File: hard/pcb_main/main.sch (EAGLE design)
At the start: 19 parts

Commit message: nop
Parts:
- added JP1, JP2, JP3, JP4, JP5, JP6: STAND-OFF, SparkFun:STAND-OFF
- added XP1: 2X10-SHROUDED, connector:2X10-SHROUDED
- added XP2, XP3, XP4, XP5, XP6, XP7, XP8: TYCO-174053(2.54), connector:TYCO-174053(2.54)
- added XP9: TYCO-174049(2.54), connector:TYCO-174049(2.54)
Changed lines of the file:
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@@
 <setting verticaltext="up"/>
 </settings>
-<grid distance="0.1" unitdist="inch" unit="inch" style="lines" multiple="1" display="no" altdistance="0.01" altunitdist="inch" altunit="inch"/>
+<grid distance="0.1" unitdist="inch" unit="inch" style="lines" multiple="1" display="yes" altdistance="0.01" altunitdist="inch" altunit="inch"/>
 <layers>
 <layer number="1" name="Top" color="4" fill="1" visible="no" active="no"/>
@@
 <part name="DA3" library="transistor-fet" deviceset="BTS" device="6143D"/>
 <part name="D1" library="optocoupler" deviceset="TCMT4100" device=""/>
+<part name="JP1" library="SparkFun" deviceset="STAND-OFF" device=""/>
+<part name="JP2" library="SparkFun" deviceset="STAND-OFF" device=""/>
+<part name="JP3" library="SparkFun" deviceset="STAND-OFF" device=""/>
+<part name="JP4" library="SparkFun" deviceset="STAND-OFF" device=""/>
+<part name="JP5" library="SparkFun" deviceset="STAND-OFF" device=""/>
+<part name="JP6" library="SparkFun" deviceset="STAND-OFF" device=""/>
+<part name="XP1" library="connector" deviceset="2X10" device="-SHROUDED"/>
+<part name="XP2" library="connector" deviceset="TYCO-174053" device="(2.54)"/>
+<part name="XP3" library="connector" deviceset="TYCO-174053" device="(2.54)"/>
+<part name="XP4" library="connector" deviceset="TYCO-174053" device="(2.54)"/>
+<part name="XP5" library="connector" deviceset="TYCO-174053" device="(2.54)"/>
+<part name="XP6" library="connector" deviceset="TYCO-174053" device="(2.54)"/>
+<part name="XP7" library="connector" deviceset="TYCO-174053" device="(2.54)"/>
+<part name="XP8" library="connector" deviceset="TYCO-174053" device="(2.54)"/>
+<part name="XP9" library="connector" deviceset="TYCO-174049" device="(2.54)"/>
 </parts>
 <sheets>
@@
 </instance>
 <instance part="U$2" gate="G$1" x="-342.9" y="-15.24"/>
+<instance part="XP1" gate="G$1" x="-309.88" y="142.24" rot="MR0"/>
 </instances>
 <busses>
@@
 <attribute name="PARTNO" x="99.06" y="101.6" size="1.778" layer="96" display="off"/>
 </instance>
+<instance part="XP9" gate="G$1" x="38.1" y="142.24" rot="MR0"/>
 </instances>
 <busses>
@@
 <instance part="D1" gate=".3" x="129.54" y="358.14"/>
 <instance part="D1" gate=".4" x="152.4" y="358.14"/>
+<instance part="XP2" gate="G$1" x="53.34" y="391.16" rot="MR0"/>
+<instance part="XP3" gate="G$1" x="53.34" y="342.9" rot="MR0"/>
+<instance part="XP4" gate="G$1" x="55.88" y="294.64" rot="MR0"/>
+<instance part="XP5" gate="G$1" x="55.88" y="243.84" rot="MR0"/>
+<instance part="XP6" gate="G$1" x="55.88" y="193.04" rot="MR0"/>
+<instance part="XP7" gate="G$1" x="55.88" y="142.24" rot="MR0"/>
+<instance part="XP8" gate="G$1" x="55.88" y="96.52" rot="MR0"/>
 </instances>
 <busses>
@@
 </nets>
 </sheet>
+<sheet>
+<description>hidden devices</description>
+<plain>
+</plain>
+<instances>
+<instance part="JP1" gate="G$1" x="0" y="48.26"/>
+<instance part="JP2" gate="G$1" x="0" y="40.64"/>
+<instance part="JP3" gate="G$1" x="0" y="33.02"/>
+<instance part="JP4" gate="G$1" x="0" y="25.4"/>
+<instance part="JP5" gate="G$1" x="0" y="17.78"/>
+<instance part="JP6" gate="G$1" x="0" y="10.16"/>
+</instances>
+<busses>
+</busses>
+<nets>
+</nets>
+</sheet>

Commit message: nop
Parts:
- added C4: 1uF/16V, rcl:C-EUC0603
- added R10: 1kOhm, rcl:R-EU_R2512
- added R8: 10kOhm, rcl:R-EU_R0603
- added R9: 100kOhm, rcl:R-EU_R0603
- added VD3: 30V, diode:SMBJ_BIDIR
- added XP10: TYCO-174049(2.54), connector:TYCO-174049(2.54)
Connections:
- new net AGND: C4.2, DD1.VREF-, DD1.VSS_A, R8.1
- new net AN_FILTERED_0: C4.1, DD1.PA0(WKUP/USART2_CTS/ADC123_IN0/TIM2_CH1_ETR/TIM5_CH1/TIM8_ETR), R8.2, R9.2
- new net AN_RAW_0: R10.2, R9.1, VD3.A1, XP8.1
- net +24V: now also R10.1
- net GND: now also VD3.A2

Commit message: alalog inputs routed
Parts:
- added C10, C11, C12, C13, C14, C15, C16, C17, C18, C19, C20, C21, C22, C8, C9: 1uF/16V, rcl:C-EUC0603
- added C23, C24, C25, C26, C27, C7: 0.1uF, rcl:C-EUC0603
- added C5, C6: 22pF, rcl:C-EUC0603
- added R11: 390Ohm, rcl:R-EU_R0603
- added R12, R13, R14, R15, R16, R17, R18, R19, R20, R25, R28, R31, R34, R37, R40, R43, R46, R49, R52, R55, R58, R61, R64, R67: 10kOhm, rcl:R-EU_R0603
- added R21, R22, R26, R29, R32, R35, R38, R41, R44, R47, R50, R53, R56, R59, R62, R65, R68: 100kOhm, rcl:R-EU_R0603
- added R23, R24: 100Ohm, rcl:R-EU_R0603
- added R27, R30, R33, R36, R39, R42, R45, R48, R51, R54, R57, R60, R63, R66, R69: 1kOhm, rcl:R-EU_R2512
- added VD10, VD11, VD12, VD13, VD14, VD15, VD16, VD17, VD18, VD19, VD20, VD6, VD7, VD8, VD9: 30V, diode:TVS-BIDIR-SMBJ30CA
- added VD4, VD5: (no value), led:LED0805
- added XP11: BOOT_0, connector:PLD_1X03
- added XP12: BOOT_1, connector:PLD_1X03
- added ZQ1: 8MHz, crystal:CRYSTALHC49UV
- VD3: device diode:SMBJ_BIDIR -> diode:TVS-BIDIR-SMBJ30CA
- XP1: value 2X10-SHROUDED -> JTAG; device connector:2X10-SHROUDED -> connector:PLD_2X10-SHROUDED
- XP10: value TYCO-174049(2.54) -> FREQUENCY
- XP2: value TYCO-174053(2.54) -> DISCRETE(1..16)
- XP3: value TYCO-174053(2.54) -> DISCRETE(49..64)
- XP4: value TYCO-174053(2.54) -> DISCRETE(17..32)
- XP5: value TYCO-174053(2.54) -> DISCRETE(33..48)
- XP6: value TYCO-174053(2.54) -> INTERFACES
- XP7: value TYCO-174053(2.54) -> OUTPUT
- XP8: value TYCO-174053(2.54) -> ANALOG
- XP9: value TYCO-174049(2.54) -> POWER
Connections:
- new net +3V3: C23.1, C24.1, C25.1, C26.1, C27.1, DD1.VDD_1, DD1.VDD_2, DD1.VDD_3, DD1.VDD_4, DD1.VDD_5, DD1.V_BAT, R13.2, R14.2, R15.2, R16.2, R17.2, R20.2, XP1.1, XP1.2, XP11.1, XP12.1
- new net AN_FILTERED_1: C8.1, DD1.PC1(ADC123_IN11), R25.2, R26.2
- new net AN_FILTERED_10: C17.1, DD1.PC4(ADC12_IN14), R52.2, R53.2
- new net AN_FILTERED_11: C18.1, DD1.PA6(SPI1_MISO/TIM8_BKIN/ADC12_IN6/TIM3_CH1/TIM1_BKIN), R55.2, R56.2
- new net AN_FILTERED_12: C19.1, DD1.PA7(SPI1_MOSI/TIM8_CH1N/ADC12_IN7/TIM3_CH2/TIM1_CH1N), R58.2, R59.2
- new net AN_FILTERED_13: C20.1, DD1.PC5(ADC12_IN15), R61.2, R62.2
- new net AN_FILTERED_14: C21.1, DD1.PB1(ADC12_IN9/TIM3_CH4/TIM8_CH3N/TIM1_CH3N), R64.2, R65.2
- new net AN_FILTERED_15: C22.1, DD1.PB0(ADC12_IN8/TIM3_CH3/TIM8_CH2N/TIM1_CH2N), R67.2, R68.2
- new net AN_FILTERED_2: C9.1, DD1.PA0(WKUP/USART2_CTS/ADC123_IN0/TIM2_CH1_ETR/TIM5_CH1/TIM8_ETR), R28.2, R29.2
- new net AN_FILTERED_3: C10.1, DD1.PC2(ADC123_IN12), R31.2, R32.2
- new net AN_FILTERED_4: C11.1, DD1.PC3(ADC123_IN13), R34.2, R35.2
- new net AN_FILTERED_5: C12.1, DD1.PA1(USART2_RTS/ADC123_IN1/TIM5_CH2/TIM2_CH2), R37.2, R38.2
- new net AN_FILTERED_6: C13.1, DD1.PA3(USART2_RX/ADC123_IN3/TIM5_CH4/TIM2_CH4), R40.2, R41.2
- new net AN_FILTERED_7: C14.1, DD1.PA2(USART2_TX/ADC123_IN2/TIM5_CH3/TIM2_CH3), R43.2, R44.2
- new net AN_FILTERED_8: C15.1, DD1.PA4(SPI1_NSS/USART2_CK/DAC1/ADC12_IN4), R46.2, R47.2
- new net AN_FILTERED_9: C16.1, DD1.PA5(SPI1_SCK/DAC2/ADC12_IN5), R49.2, R50.2
- new net AN_RAW_1: R26.1, R27.2, VD6.A1, XP8.2
- new net AN_RAW_10: R53.1, R54.2, VD15.A1, XP8.14
- new net AN_RAW_11: R56.1, R57.2, VD16.A1, XP8.13
- new net AN_RAW_12: R59.1, R60.2, VD17.A1, XP8.7
- new net AN_RAW_13: R62.1, R63.2, VD18.A1, XP8.8
- new net AN_RAW_14: R65.1, R66.2, VD19.A1, XP8.16
- new net AN_RAW_15: R68.1, R69.2, VD20.A1, XP8.15
- new net AN_RAW_2: R29.1, R30.2, VD7.A1, XP8.10
- new net AN_RAW_3: R32.1, R33.2, VD8.A1, XP8.9
- new net AN_RAW_4: R35.1, R36.2, VD9.A1, XP8.3
- new net AN_RAW_5: R38.1, R39.2, VD10.A1, XP8.4
- new net AN_RAW_6: R41.1, R42.2, VD11.A1, XP8.12
- new net AN_RAW_7: R44.1, R45.2, VD12.A1, XP8.11
- new net AN_RAW_8: R47.1, R48.2, VD13.A1, XP8.5
- new net AN_RAW_9: R50.1, R51.2, VD14.A1, XP8.6
- new net BOOT_0: DD1.BOOT_0, R22.1
- new net BOOT_1: DD1.PB2(BOOT_1)*, R21.1, R21.2, VD5.A, XP12.2
- new net JTCK: DD1.JTCK/SWCLK(PA14)*, R15.1, XP1.9
- new net JTDI: DD1.JTDI(PA15/SPI3_NSS/I2S3_WS/TIM2_CH1_ETR/SPI1_NSS)*, R16.1, XP1.5
- new net JTDO: DD1.JTDO(PB3/SPI3_SCK/I2S3_CK/TRACEWO/TIM2_CH2/SPI1_SCK)*, R14.1, XP1.13
- new net JTMS: DD1.JTMS/SWDIO(PA13)*, R17.1, XP1.7
- new net JTRST: DD1.NJTRST(PB4/SPI3_MISO/TIM3_CH1/SPI1_MISO)*, R13.1, XP1.3
- new net N$12: R12.1, XP1.19
- new net N$13: R18.1, XP1.17
- new net N$14: DD1.OSC_OUT, R11.2
- new net N$15: C5.1, DD1.OSC_IN, ZQ1.P$2
- new net N$16: C6.1, R11.1, ZQ1.P$1
- new net N$17: R19.1, XP1.11
- new net N$18: R22.2, VD4.A, XP11.2
- new net N$19: R23.2, VD4.C
- new net N$20: R24.2, VD5.C
- new net N$21: XP9.4, XP9.5, XP9.6, XP9.7, XP9.8
- new net RST: C7.1, DD1.NRST, R20.1, XP1.15
- net +24V: now also R27.1, R30.1, R33.1, R36.1, R39.1, R42.1, R45.1, R48.1, R51.1, R54.1, R57.1, R60.1, R63.1, R66.1, R69.1
- net AGND: now also C10.2, C11.2, C12.2, C13.2, C14.2, C15.2, C16.2, C17.2, C18.2, C19.2, C20.2, C21.2, C22.2, C8.2, C9.2, R25.1, R28.1, R31.1, R34.1, R37.1, R40.1, R43.1, R46.1, R49.1, R52.1, R55.1, R58.1, R61.1, R64.1, R67.1
- net AN_FILTERED_0: now also DD1.PC0(ADC123_IN10); no longer DD1.PA0(WKUP/USART2_CTS/ADC123_IN0/TIM2_CH1_ETR/TIM5_CH1/TIM8_ETR)
- net GND: now also C23.2, C24.2, C25.2, C26.2, C27.2, C5.2, C6.2, C7.2, DD1.VSS_1, DD1.VSS_2, DD1.VSS_3, DD1.VSS_4, DD1.VSS_5, R12.2, R18.2, R19.2, R23.1, R24.1, VD10.A2, VD11.A2, VD12.A2, VD13.A2, VD14.A2, VD15.A2, VD16.A2, VD17.A2, VD18.A2, VD19.A2, VD20.A2, VD6.A2, VD7.A2, VD8.A2, VD9.A2, XP1.10, XP1.12, XP1.14, XP1.16, XP1.18, XP1.20, XP1.4, XP1.6, XP1.8, XP11.3, XP12.3

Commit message: almost ready schematic of power supply
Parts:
- added C28: 0.01uF, rcl:C-EUC0805
- added C29: 0.1uF, rcl:C-EUC0603
- added DA4: MC33091A, driver-fet:MC33091A
- added R70: 1kOhm, rcl:R-EU_R0805
- added R71: 3.3kOhm, rcl:R-EU_R2512
- added VD21: 1000V/3A, diode:DIODE-STANDARD-SMC
- added VD22: SM6T220A, diode:DIODE-TVS-UNIDIR-SMB
- added VD23, VD24, VD25, VD27: SMBJ28CA, diode:DIODE-TVS-BIDIR-SMB
- added VD26: SM6T6V8A, diode:DIODE-TVS-UNIDIR-SMB
- added VT1: IRFR430, transistor-fet:IRFR430
- C23, C24, C25, C26, C27, C7: PARTNO (none) -> C0603C104K5RACTU
- C5, C6: PARTNO (none) -> C0603C220J5GACTU
- D1, DA3, VD4, VD5, XP1, XP10, XP11, XP12, XP2, XP3, XP4, XP5, XP6, XP7, XP8, XP9: PARTNO (none) -> *
- DA1, DA2: value LM2596S -> LM2596S-5.0; device vreg:LM2596S -> vreg:LM2596S-5.0; PARTNO LM2596S-ADJ -> LM2596S-5.0
- JP1, JP2, JP3, JP4, JP5, JP6: BOM (none) -> EXCLUDE
- R1: value 15kOhm -> 100kOhm; device rcl:R-EU_R0805 -> rcl:R-EU_R0603; PARTNO ERJ6GEYJ153V -> RC0603FR-13100KL
- R11: PARTNO (none) -> ERJ3GEYJ391V
- R12, R13, R14, R15, R16, R17, R18, R19, R20: PARTNO (none) -> RC0603FR-1010KL
- R2: value 3.3kOhm -> 15kOhm; PARTNO ERJ6GEYJ332V -> ERJ6GEYJ153V
- R21, R22: PARTNO (none) -> RC0603FR-13100KL
- R23, R24: PARTNO (none) -> ERJ3GEYJ101V
- R3: value 15kOhm -> 82kOhm; PARTNO ERJ6GEYJ153V -> RC0805JR-0782KL
- R4: value 3.3kOhm -> 470kOhm; PARTNO ERJ6GEYJ332V -> ERJ6GEYJ474V
- VD10, VD11, VD12, VD13, VD15, VD16, VD17, VD18, VD19, VD20, VD3, VD6, VD7, VD8, VD9: value 30V -> SMBJ28CA; device diode:TVS-BIDIR-SMBJ30CA -> diode:DIODE-TVS-BIDIR-SMB; PARTNO (none) -> SMBJ28CA-TR
- VD14: value 30V -> SMBJ28CA; device diode:TVS-BIDIR-SMBJ30CA -> diode:DIODE-TVS-BIDIR-SMB; PARTNO (none) -> SMBJ30CA
- ZQ1: PARTNO (none) -> CA-4.000-18-3050-X
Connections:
- removed net +6V3: C3.+, L1.2, R3.2
- removed net -6V3: C1.-, DA2.!ON!/OFF, DA2.GND, DA2.GND@6, R2.1, VD2.A
- new net +24V_CLEAR: C2.+, DA1.VIN, DA2.VIN, R10.1, R27.1, R30.1, R33.1, R36.1, R39.1, R42.1, R45.1, R48.1, R51.1, R54.1, R57.1, R60.1, R63.1, R66.1, R69.1, VD27.A1, VT1.S
- new net +5V: C3.+, DA1.FB, L1.2
- new net -5V: C1.-, DA2.!ON!/OFF, DA2.GND, DA2.GND@6, VD2.A
- new net N$22: VD22.C, VD23.A2
- new net N$23: VD24.A1, VD25.A2
- new net N$24: DA4.DRN, R3.2, VD24.A2
- new net N$25: DA4.IN, R1.1, R2.2, VD26.C
- new net N$26: R2.1, R3.1, R71.2, VD21.C, VT1.D
- new net N$27: DA4.SRC, R70.1
- new net N$28: C28.1, DA4.VT, R4.2
- new net N$29: R70.2, VT1.G
- net +24V: now also VD21.A, VD23.A1, XP9.1, XP9.2, XP9.3, XP9.4; no longer C2.+, DA1.VIN, DA2.VIN, R10.1, R27.1, R30.1, R33.1, R36.1, R39.1, R42.1, R45.1, R48.1, R51.1, R54.1, R57.1, R60.1, R63.1, R66.1, R69.1
- net AN_RAW_0: now also XP8.10; no longer XP8.1
- net AN_RAW_1: now also XP8.11; no longer XP8.2
- net AN_RAW_11: now also XP8.6; no longer XP8.13
- net AN_RAW_13: now also XP8.15; no longer XP8.8
- net AN_RAW_14: now also XP8.9; no longer XP8.16
- net AN_RAW_15: now also XP8.8; no longer XP8.15
- net AN_RAW_2: no longer XP8.10
- net AN_RAW_3: now also XP8.12; no longer XP8.9
- net AN_RAW_4: now also XP8.13; no longer XP8.3
- net AN_RAW_5: now also XP8.1; no longer XP8.4
- net AN_RAW_6: now also XP8.3; no longer XP8.12
- net AN_RAW_7: now also XP8.2; no longer XP8.11
- net AN_RAW_8: now also XP8.4; no longer XP8.5
- net AN_RAW_9: now also XP8.5; no longer XP8.6
- net GND: now also C28.2, C29.2, DA2.FB, DA4.GND, VD22.A, VD25.A1, VD26.A, VD27.A2, XP8.16, XP9.5, XP9.6, XP9.7, XP9.8
- net N$1: now also DA3.IN, R6.1; no longer DA1.FB, R3.1, R4.2
- net N$21: now also C29.1, DA4.VCC, R71.1; no longer XP9.4, XP9.5, XP9.6, XP9.7, XP9.8
- net N$5: now also R6.2, R7.1; no longer DA2.FB, R1.1, R2.2
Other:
- note added: "fuse 0.5A"
- note added: "fuse 2A"
- moved on the sheet: C1, C2, C3, DA1, DA2, L1, L2, R1, R2, R3, R4, VD1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

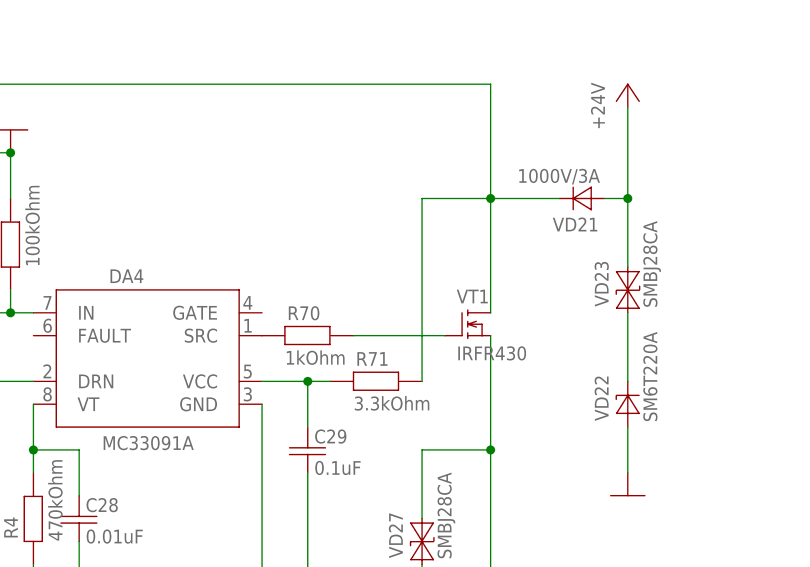
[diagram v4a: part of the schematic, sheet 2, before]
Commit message: loaddump protection placed
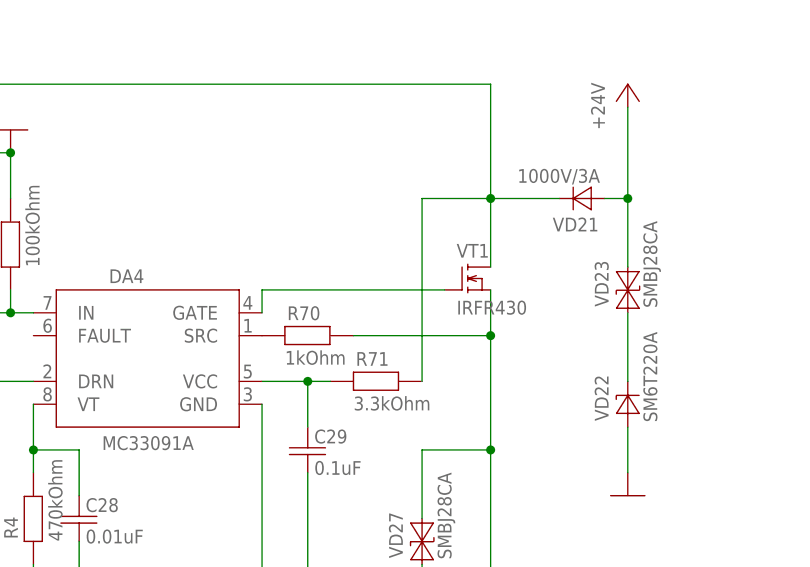
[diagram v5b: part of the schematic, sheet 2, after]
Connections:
- net +24V_CLEAR: now also R70.2
- net N$29: now also DA4.GATE; no longer R70.2
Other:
- moved on the sheet: VT1
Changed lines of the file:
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@@
 </instance>
 <instance part="GND35" gate="1" x="104.14" y="127"/>
-<instance part="VT1" gate="G$1" x="109.22" y="162.56">
-<attribute name="PARTNO" x="109.22" y="162.56" size="1.778" layer="96" display="off"/>
+<instance part="VT1" gate="G$1" x="109.22" y="167.64">
+<attribute name="PARTNO" x="109.22" y="167.64" size="1.778" layer="96" display="off"/>
 </instance>
 </instances>
@@
 </segment>
 <segment>
-<wire x1="111.76" y1="160.02" x2="111.76" y2="147.32" width="0.1524" layer="91"/>
+<wire x1="111.76" y1="165.1" x2="111.76" y2="160.02" width="0.1524" layer="91"/>
 <pinref part="P+21" gate="G$1" pin="+24V_CLEAR"/>
 <pinref part="VD27" gate="G$1" pin="A1"/>
+<wire x1="111.76" y1="160.02" x2="111.76" y2="147.32" width="0.1524" layer="91"/>
 <wire x1="111.76" y1="147.32" x2="111.76" y2="127" width="0.1524" layer="91"/>
 <wire x1="104.14" y1="139.7" x2="104.14" y2="147.32" width="0.1524" layer="91"/>
@@
 <junction x="111.76" y="147.32"/>
 <pinref part="VT1" gate="G$1" pin="S"/>
+<pinref part="R70" gate="G$1" pin="2"/>
+<wire x1="111.76" y1="160.02" x2="96.52" y2="160.02" width="0.1524" layer="91"/>
+<junction x="111.76" y="160.02"/>
 </segment>
 </net>
@@
 <pinref part="VD21" gate="G$1" pin="C"/>
 <wire x1="119.38" y1="175.26" x2="111.76" y2="175.26" width="0.1524" layer="91"/>
-<wire x1="111.76" y1="175.26" x2="111.76" y2="162.56" width="0.1524" layer="91"/>
+<wire x1="111.76" y1="175.26" x2="111.76" y2="167.64" width="0.1524" layer="91"/>
 <pinref part="R71" gate="G$1" pin="2"/>
 <wire x1="104.14" y1="154.94" x2="104.14" y2="175.26" width="0.1524" layer="91"/>
@@
 <net name="N$29" class="0">
 <segment>
-<pinref part="R70" gate="G$1" pin="2"/>
-<wire x1="106.68" y1="160.02" x2="96.52" y2="160.02" width="0.1524" layer="91"/>
 <pinref part="VT1" gate="G$1" pin="G"/>
-</segment>
-</net>
+<pinref part="DA4" gate="G$1" pin="GATE"/>
+<wire x1="106.68" y1="165.1" x2="86.36" y2="165.1" width="0.1524" layer="91"/>
+<wire x1="86.36" y1="165.1" x2="86.36" y2="162.56" width="0.1524" layer="91"/>
+</segment>
+</net>
